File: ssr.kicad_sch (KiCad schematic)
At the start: 6 parts, among them Q4 Q_NMOS_DGS, U1 10A SSR

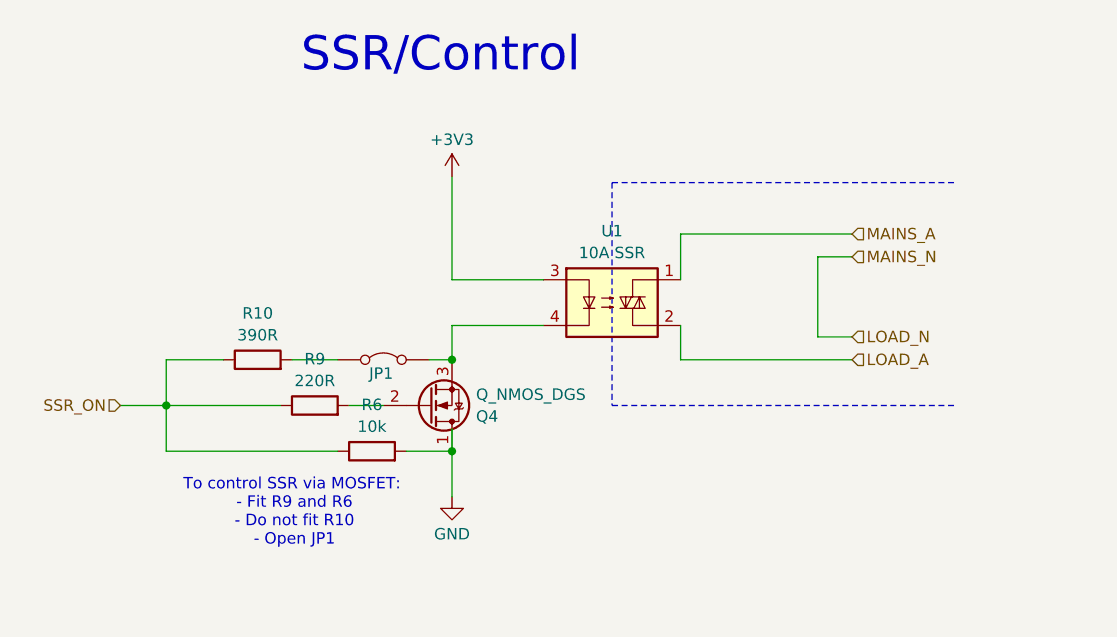
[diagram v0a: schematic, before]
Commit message: Added fuses to SSRs
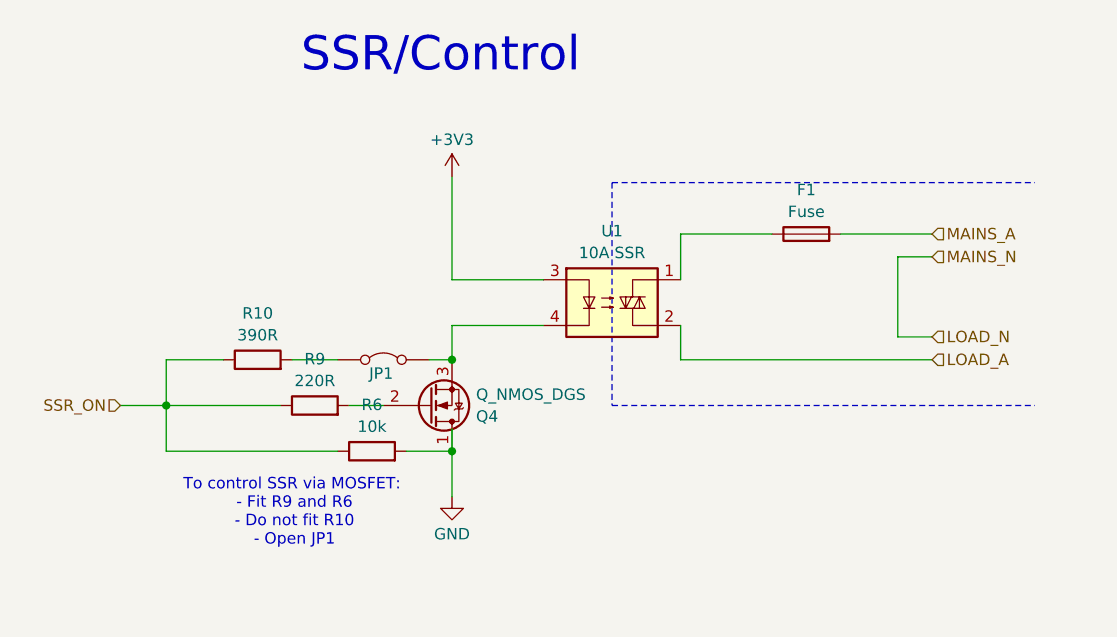
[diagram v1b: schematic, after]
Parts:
- added F1: Fuse, symbol Device:Fuse
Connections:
- net MAINS_A: now also F1.2; no longer U1.1
- new net: F1.1, U1.1
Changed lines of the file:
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@@
 	(wire
 		(pts
-			(xy 162.56 85.09) (xy 162.56 76.2)
+			(xy 171.45 85.09) (xy 171.45 76.2)
 		)
 		(stroke
@@
 	(wire
 		(pts
-			(xy 147.32 87.63) (xy 166.37 87.63)
+			(xy 147.32 87.63) (xy 175.26 87.63)
 		)
 		(stroke
@@
 	(polyline
 		(pts
-			(xy 139.7 92.71) (xy 177.8 92.71)
+			(xy 139.7 92.71) (xy 186.69 92.71)
 		)
 		(stroke
@@
 	(wire
 		(pts
-			(xy 166.37 85.09) (xy 162.56 85.09)
+			(xy 175.26 85.09) (xy 171.45 85.09)
 		)
 		(stroke
@@
 	(wire
 		(pts
-			(xy 166.37 73.66) (xy 147.32 73.66)
+			(xy 175.26 73.66) (xy 165.1 73.66)
 		)
 		(stroke
@@
 	(polyline
 		(pts
-			(xy 139.7 67.945) (xy 177.8 67.945)
+			(xy 139.7 67.945) (xy 186.69 67.945)
 		)
 		(stroke
@@
 	(wire
 		(pts
-			(xy 162.56 76.2) (xy 166.37 76.2)
+			(xy 157.48 73.66) (xy 147.32 73.66)
+		)
+		(stroke
+			(width 0)
+			(type default)
+		)
+	)
+	(wire
+		(pts
+			(xy 171.45 76.2) (xy 175.26 76.2)
 		)
 		(stroke
@@
 	(hierarchical_label "LOAD_A"
 		(shape input)
-		(at 166.37 87.63 0)
+		(at 175.26 87.63 0)
 		(fields_autoplaced yes)
 		(effects
@@
 	(hierarchical_label "LOAD_N"
 		(shape input)
-		(at 166.37 85.09 0)
+		(at 175.26 85.09 0)
 		(fields_autoplaced yes)
 		(effects
@@
 	(hierarchical_label "MAINS_N"
 		(shape input)
-		(at 166.37 76.2 0)
+		(at 175.26 76.2 0)
 		(fields_autoplaced yes)
 		(effects
@@
 	(hierarchical_label "MAINS_A"
 		(shape input)
-		(at 166.37 73.66 0)
+		(at 175.26 73.66 0)
 		(fields_autoplaced yes)
 		(effects
@@
 					(unit 1)
 				)
+			)
+		)
+	)
+	(symbol
+		(lib_id "Device:Fuse")
+		(at 161.29 73.66 90)
+		(unit 1)
+		(exclude_from_sim no)
+		(in_bom yes)
+		(on_board yes)
+		(dnp no)
+		(fields_autoplaced yes)
+		(property "Reference" "F1"
+			(at 161.29 68.7535 90)
+			(effects
+				(font
+					(size 1.27 1.27)
+				)
+			)
+		)
+		(property "Value" "Fuse"
+			(at 161.29 71.1778 90)
+			(effects
+				(font
+					(size 1.27 1.27)
+				)
+			)
+		)
+		(property "Footprint" ""
+			(at 161.29 75.438 90)
+			(effects
+				(font
+					(size 1.27 1.27)
+				)
+				(hide yes)
+			)
+		)
+		(property "Datasheet" "~"
+			(at 161.29 73.66 0)
+			(effects
+				(font
+					(size 1.27 1.27)
+				)
+				(hide yes)
+			)
+		)
+		(property "Description" "Fuse"
+			(at 161.29 73.66 0)
+			(effects
+				(font
+					(size 1.27 1.27)
+				)
+				(hide yes)
+			)
+		)
+		(pin "2"
+		)
+		(pin "1"
+		)
+		(instances
+			(project "board-burner"
+				(path "/8e8c1c81-e974-4404-a855-b409907250d2/ff0e7100-4e2e-4758-a58c-100462f0abae"
+					(reference "F1")
+					(unit 1)
+				)
+				(path "/8e8c1c81-e974-4404-a855-b409907250d2/978f5725-fdb0-40aa-a547-4154f864a506"
+					(reference "F2")
+					(unit 1)
+				)
+				(path "/8e8c1c81-e974-4404-a855-b409907250d2/6c0544fa-e726-4e16-b2f3-fde221c87365"
+					(reference "F3")
+					(unit 1)
+				)

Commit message: Further work, most components now present
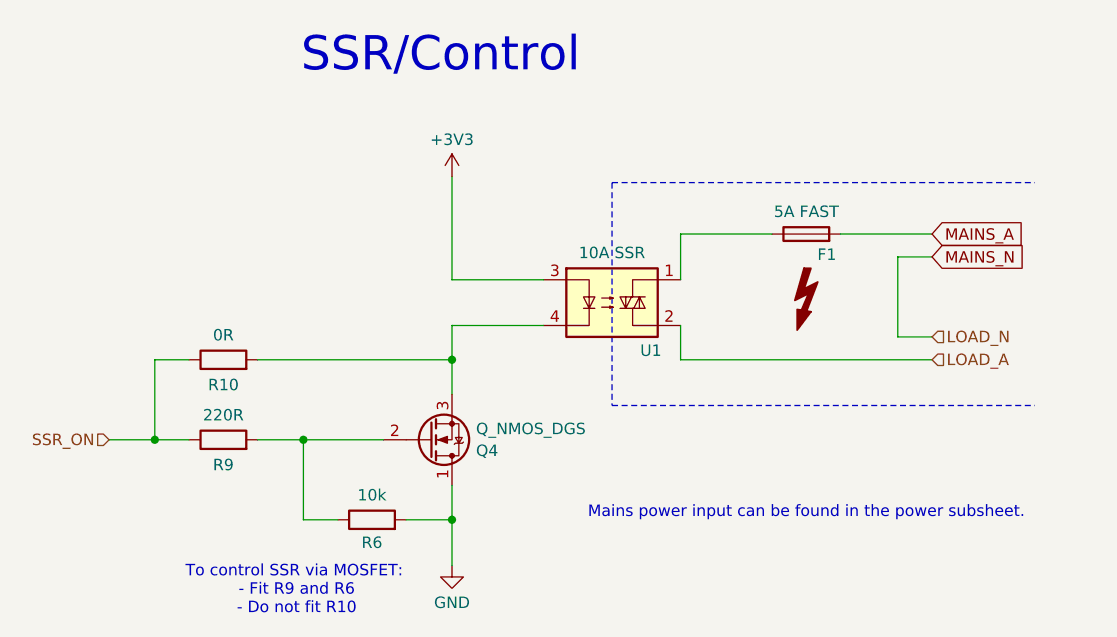
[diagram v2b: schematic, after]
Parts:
- removed JP1: Jumper_2_Bridged, symbol Jumper:Jumper_2_Bridged
- F1: value Fuse -> 5A FAST
- R10: value 390R -> 0R
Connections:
- net SSR_ON: no longer R6.1
- net at Q4.2 (G), R9.2: now also R6.1
- net at Q4.3 (S), U1.4: now also R10.2
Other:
- note added: "Mains power input can be found in the power subsheet."
- note added: "To control SSR via MOSFET: - Fit R9 and R6 - Do not fit R10"
- note removed: "To control SSR via MOSFET: - Fit R9 and R6 - Do not fit R10 - Open JP1"
- moved on the sheet: Q4, R10, R6, R9
